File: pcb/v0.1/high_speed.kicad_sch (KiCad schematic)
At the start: 22 parts, among them J4 TYPE_C_Receptacle, J5 TYPE_C_Receptacle, J6 22s_disp_connector, J7 ComputeModule5-CM5_connector, U2 Nexperia PUSB3FR4Z, U3 Nexperia PUSB3FR4Z, U8 AP22653W6-7

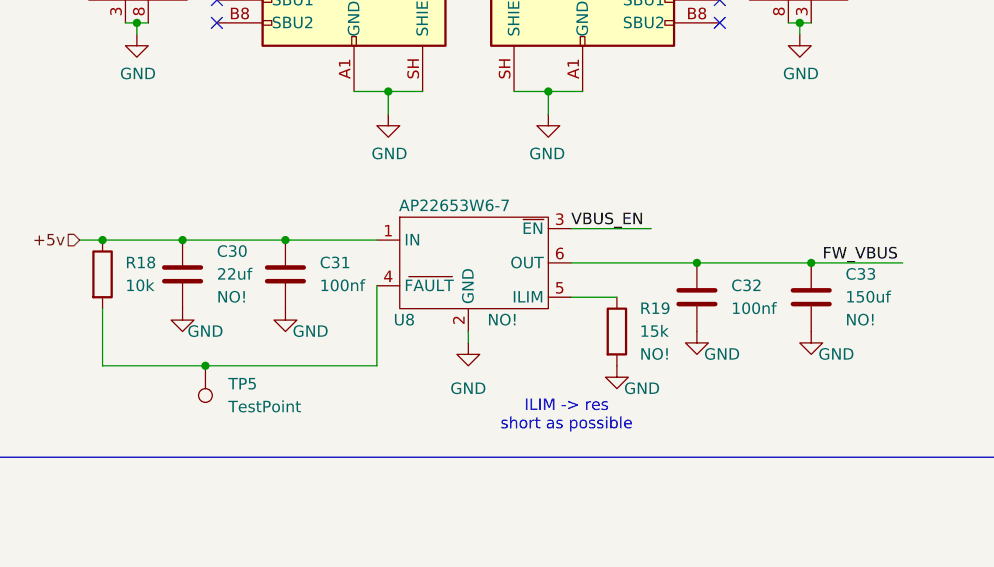
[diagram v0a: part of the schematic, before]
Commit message: Assigned all the footprints
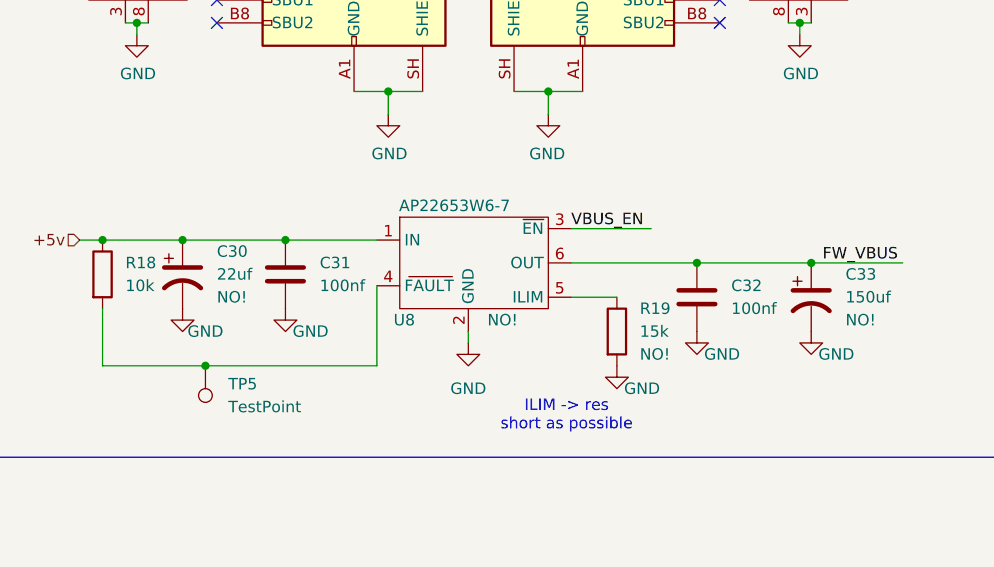
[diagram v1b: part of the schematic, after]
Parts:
- C30: footprint (none) -> Capacitor_SMD:CP_Elec_5x5.3
- C33: footprint (none) -> Capacitor_SMD:CP_Elec_8x10.5
- J4, J5: footprint (none) -> Connector_USB:USB_C_Receptacle_Molex_105450-0101
- J6: footprint (none) -> Connector_PinHeader_2.54mm:PinHeader_1x04_P2.54mm_Vertical
- J7: footprint (none) -> CM5IO:Raspberry-Pi-5-Compute-Module
- TP5: footprint (none) -> TestPoint:TestPoint_Pad_D1.0mm
- U2, U3: footprint (none) -> Package_DFN_QFN:Diodes_UDFN-10_1x2.5mm_P0.5mm
- U8: footprint (none) -> Package_TO_SOT_SMD:SOT-23-6
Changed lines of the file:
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@@
 			)
 		)
-		(property "Footprint" ""
+		(property "Footprint" "Connector_USB:USB_C_Receptacle_Molex_105450-0101"
 			(at 200.66 58.42 0)
 			(hide yes)
@@
 			)
 		)
-		(property "Footprint" ""
+		(property "Footprint" "Capacitor_SMD:CP_Elec_5x5.3"
 			(at 186.3852 123.19 0)
 			(hide yes)
@@
 			)
 		)
-		(property "Footprint" ""
+		(property "Footprint" "Package_DFN_QFN:Diodes_UDFN-10_1x2.5mm_P0.5mm"
 			(at 247.65 71.12 0)
 			(hide yes)
@@
 			)
 		)
-		(property "Footprint" ""
+		(property "Footprint" "Package_TO_SOT_SMD:SOT-23-6"
 			(at 209.55 113.03 0)
 			(hide yes)
@@
 			)
 		)
-		(property "Footprint" ""
+		(property "Footprint" "Capacitor_SMD:CP_Elec_8x10.5"
 			(at 256.2352 125.73 0)
 			(hide yes)
@@
 			)
 		)
-		(property "Footprint" ""
+		(property "Footprint" "CM5IO:Raspberry-Pi-5-Compute-Module"
 			(at 67.31 115.57 0)
 			(hide yes)
@@
 			)
 		)
-		(property "Footprint" ""
+		(property "Footprint" "Connector_USB:USB_C_Receptacle_Molex_105450-0101"
 			(at 233.68 58.42 0)
 			(hide yes)
@@
 			)
 		)
-		(property "Footprint" ""
+		(property "Footprint" "TestPoint:TestPoint_Pad_D1.0mm"
 			(at 182.88 129.54 0)
 			(hide yes)
@@
 			)
 		)
-		(property "Footprint" ""
+		(property "Footprint" "Package_DFN_QFN:Diodes_UDFN-10_1x2.5mm_P0.5mm"
 			(at 186.69 71.12 0)
 			(hide yes)
@@
 			)
 		)
-		(property "Footprint" ""
+		(property "Footprint" "Connector_PinHeader_2.54mm:PinHeader_1x04_P2.54mm_Vertical"
 			(at 140.97 190.5 0)
 			(hide yes)

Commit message: Board setup and basic layout grouping
* Added board setup settings according to JLCpcbs manufacturing minimums
  (and generous extra)
* Grouped related components on the pcb
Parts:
- J6: footprint Connector_PinHeader_2.54mm:PinHeader_1x04_P2.54mm_Vertical -> CM5IO:Hirose_FH12-22S-0.5SH_1x22-1MP_P0.50mm_Horizontal
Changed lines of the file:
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@@
 			)
 		)
-		(property "Footprint" "Connector_PinHeader_2.54mm:PinHeader_1x04_P2.54mm_Vertical"
+		(property "Footprint" "CM5IO:Hirose_FH12-22S-0.5SH_1x22-1MP_P0.50mm_Horizontal"
 			(at 140.97 190.5 0)
 			(hide yes)

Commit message: Remove USB Type-c ports + minor changes + dru file
The current USB type-c ports aren't properly routable without using via
in pad, which at the current stage is prohibitively expensive. I've
removed them for now with the intent of swapping them out for ones from
GTC.

Additionally I noticed that a dru file has not been committed this whole
time. Its existed for a while on my computer.
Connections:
- net USB3-0-RX_N: now also U2.10 (NC)
- net USB3-0-RX_P: now also U2.9 (NC)
- net USB3-0-TX_N: now also U2.7 (NC)
- net USB3-0-TX_P: now also U2.6 (NC)
- net USB3-1-RX_N: now also U3.10 (NC)
- net USB3-1-RX_P: now also U3.9 (NC)
- net USB3-1-TX_N: now also U3.7 (NC)
- net USB3-1-TX_P: now also U3.6 (NC)

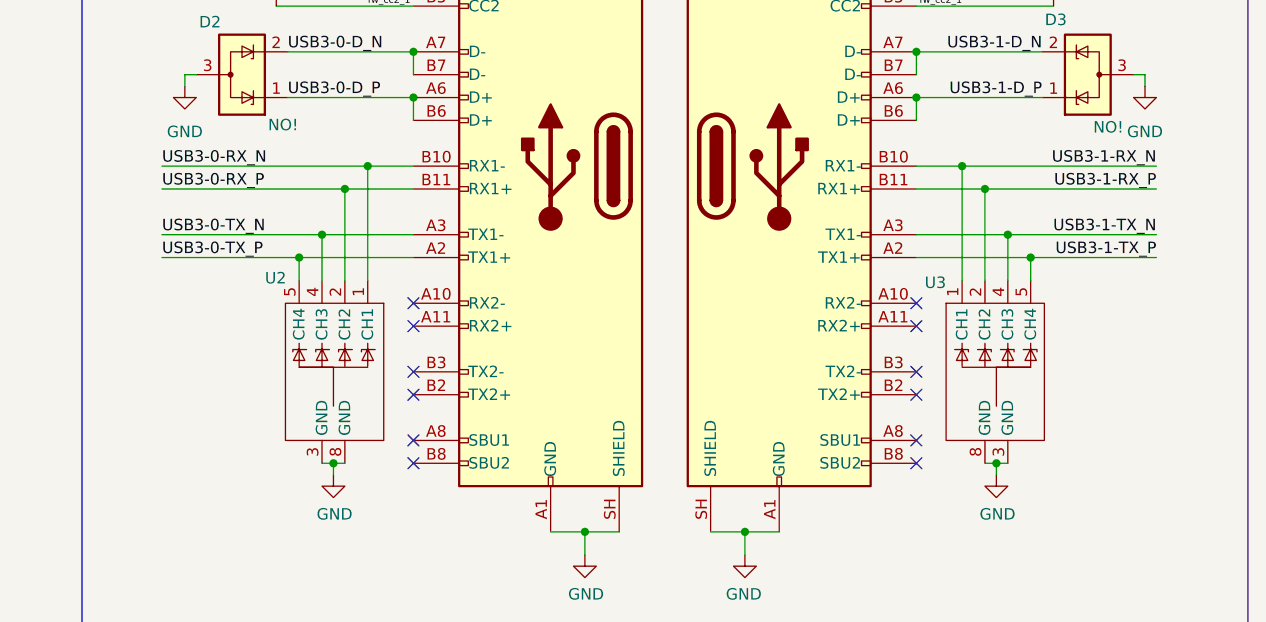
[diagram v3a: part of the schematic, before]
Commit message: USB differential pairs complete.
Had to break these out from the rest of the pcb as they just didn't add
up otherwise. Will continue to do the high speed lines separately before
re assembling the pcb.
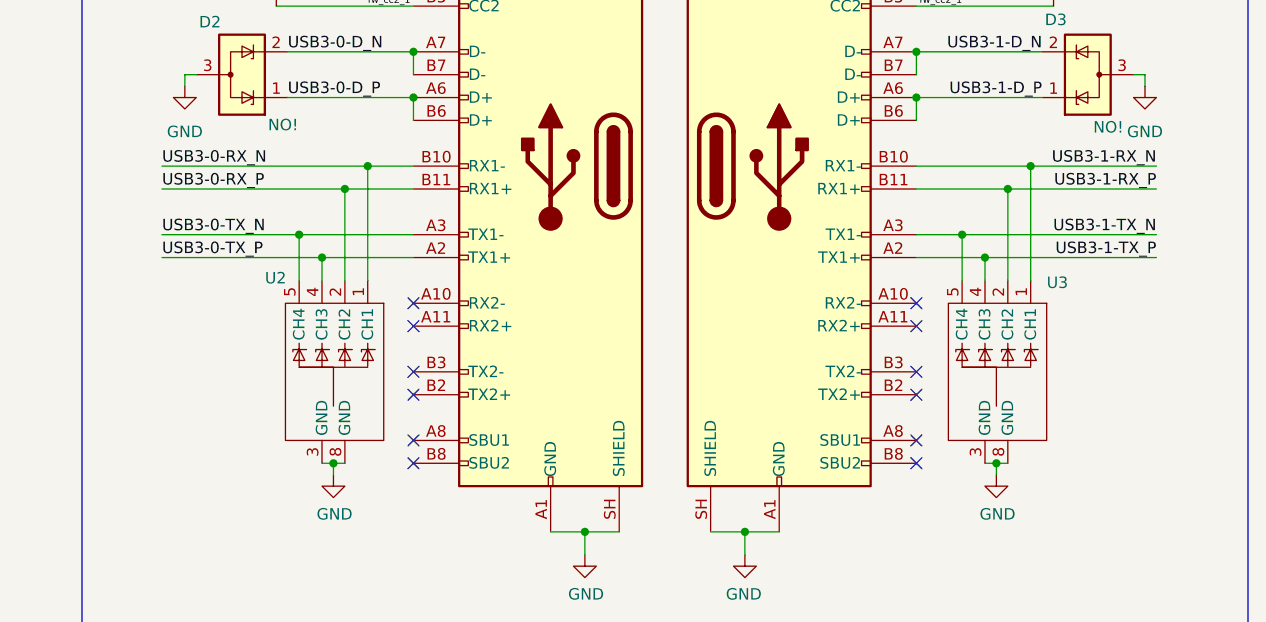
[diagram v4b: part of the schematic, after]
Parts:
- J4, J5: footprint Connector_USB:USB_C_Receptacle_Molex_105450-0101 -> TH-1-CC_footprints:USB4056-03-A; Digikey Part no WM12856TR-ND -> 2073-USB4056-03-ATR-ND; Distributor Digikey https://www.digikey.co.uk/en/products/detail/molex/10545001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 -> https://www.digikey.co.uk/en/products/detail/gct/USB4056-03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; Manufacturer MOLEX -> GCT; Mfr. Part no 1054500101 -> USB4056-03-A
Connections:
- net USB3-0-TX_N: now also U2.5 (CH4), U2.6 (NC); no longer U2.4 (CH3), U2.7 (NC)
- net USB3-0-TX_P: now also U2.4 (CH3), U2.7 (NC); no longer U2.5 (CH4), U2.6 (NC)
- net USB3-1-TX_N: now also U3.5 (CH4), U3.6 (NC); no longer U3.4 (CH3), U3.7 (NC)
- net USB3-1-TX_P: now also U3.4 (CH3), U3.7 (NC); no longer U3.5 (CH4), U3.6 (NC)
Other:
- moved on the sheet: U3

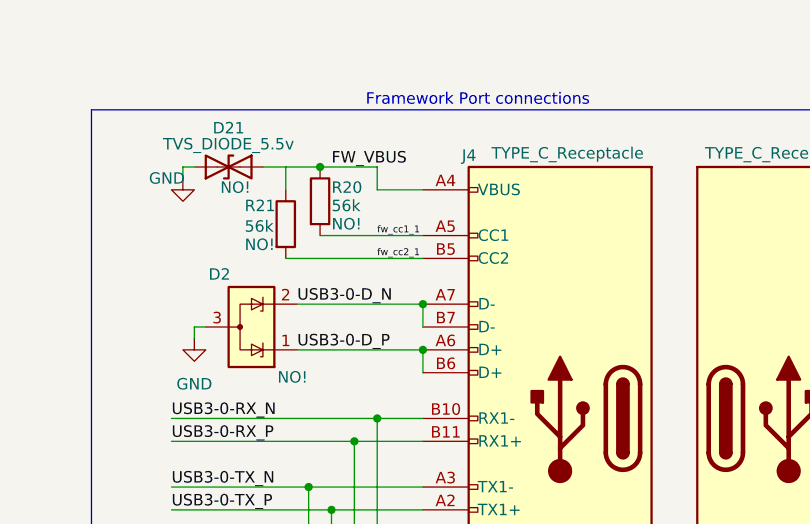
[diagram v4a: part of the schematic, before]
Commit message: New rough layout
Had to change everything up due to the requirements of the high speed
lines. The board is now also a lot smaller
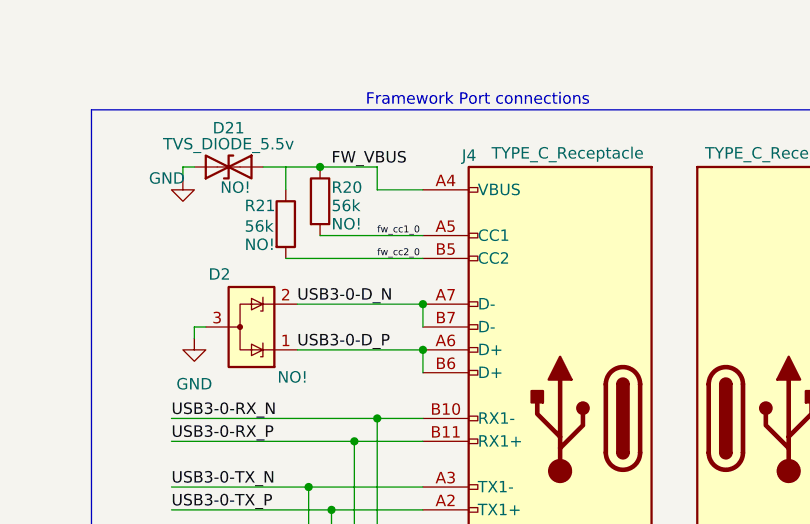
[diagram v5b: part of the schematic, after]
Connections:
- net fw_cc1_1: no longer J4.A5 (CC1), R20.2
- net fw_cc2_1: no longer J4.B5 (CC2), R21.2
- new net fw_cc1_0: J4.A5 (CC1), R20.2
- new net fw_cc2_0: J4.B5 (CC2), R21.2
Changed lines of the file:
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@@
 		)
 	)
-	(label "fw_cc2_1"
+	(label "fw_cc2_0"
 		(at 184.15 40.64 0)
 		(effects
@@
 		)
 	)
-	(label "fw_cc1_1"
+	(label "fw_cc1_0"
 		(at 184.15 38.1 0)
 		(effects

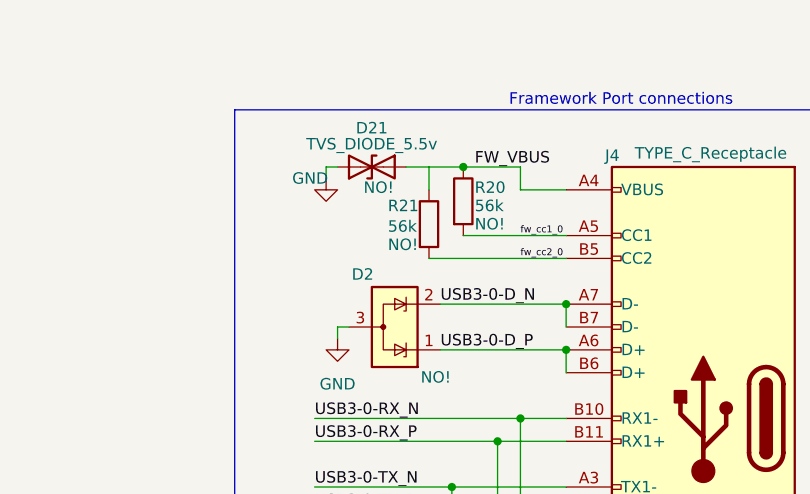
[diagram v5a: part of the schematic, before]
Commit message: A large chunk of the pcb routing + shrinking the board
Did a large chunk of the PCB routing, probably just under half of all
remaining traces. Additionally I shrank the pcb to below 100x100 as it
reduces the price of manufacturing by roughly 4x
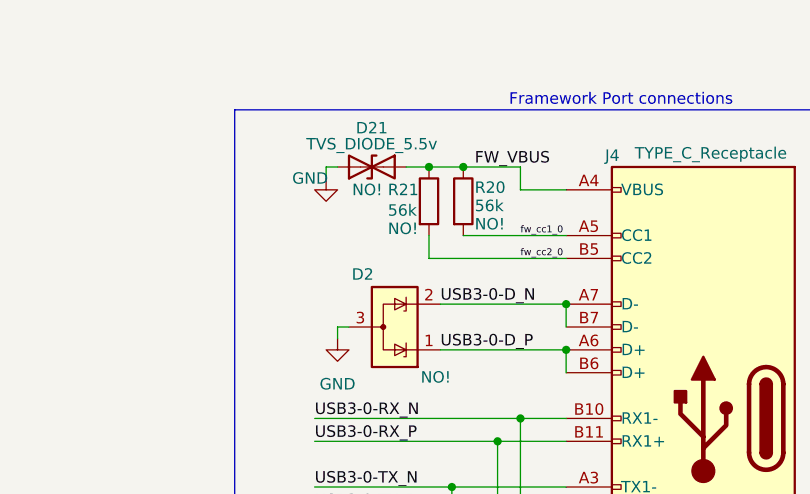
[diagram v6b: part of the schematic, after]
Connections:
- net FW_VBUS: now also R21.1
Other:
- moved on the sheet: R21
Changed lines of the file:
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@@
 	)
 	(junction
+		(at 173.99 30.48)
+		(diameter 0)
+		(color 0 0 0 0)
+	)
+	(junction
 		(at 31.75 66.04)
 		(diameter 1.016)
@@
 	(wire
 		(pts
+			(xy 173.99 30.48) (xy 177.8 30.48)
+		)
+		(stroke
+			(width 0)
+			(type default)
+		)
+	)
+	(wire
+		(pts
 			(xy 31.75 73.66) (xy 34.29 73.66)
 		)
@@
 	(wire
 		(pts
-			(xy 171.45 30.48) (xy 177.8 30.48)
+			(xy 171.45 30.48) (xy 173.99 30.48)
 		)
 		(stroke
@@
 	(wire
 		(pts
-			(xy 173.99 33.02) (xy 173.99 30.48)
+			(xy 173.99 38.1) (xy 173.99 40.64)
 		)
 		(stroke
@@
 	(wire
 		(pts
+			(xy 173.99 40.64) (xy 189.23 40.64)
+		)
+		(stroke
+			(width 0)
+			(type default)
+		)
+	)
+	(wire
+		(pts
 			(xy 242.57 118.11) (xy 255.27 118.11)
 		)
@@
 	(wire
 		(pts
-			(xy 173.99 40.64) (xy 189.23 40.64)
-		)
-		(stroke
-			(width 0)
-			(type default)
-		)
-	)
-	(wire
-		(pts
 			(xy 95.25 127) (xy 97.79 127)
 		)
@@
 	(symbol
 		(lib_id "TH-1-CC:R_56k")
-		(at 173.99 36.83 0)
+		(at 173.99 34.29 0)
 		(unit 1)
 		(body_style 1)
@@
 		(dnp no)
 		(property "Reference" "R21"
-			(at 169.418 34.798 0)
+			(at 169.418 33.02 0)
 			(show_name no)
 			(do_not_autoplace no)
@@
 		)
 		(property "Value" "56k"
-			(at 169.418 37.084 0)
+			(at 169.418 35.306 0)
 			(show_name no)
 			(do_not_autoplace no)
@@
 		)
 		(property "Footprint" "Resistor_SMD:R_0603_1608Metric"
-			(at 172.212 36.83 90)
+			(at 172.212 34.29 90)
 			(hide yes)
 			(show_name no)
@@
 		)
 		(property "Datasheet" "https://www.lcsc.com/datasheet/C114630.pdf?spm=wm.sxq.inf.ggs&lcsc_vid=EwQKAlxRFgdXV1MCRARYXwJRRVZeV1dUEgJXBQFQQgQxVlNeRVFWVVdeT1RaUzsOAxUeFF5JWBYZEEoKFBINSQcJGk4NBhADEA4cHktXRlhXSQwSGg0%3D"
-			(at 173.99 36.83 0)
+			(at 173.99 34.29 0)
 			(hide yes)
 			(show_name no)
@@
 		)
 		(property "Description" "RES 56kΩ ±1% 100mW 0603"
-			(at 173.99 36.83 0)
+			(at 173.99 34.29 0)
 			(hide yes)
 			(show_name no)
@@
 		)
 		(property "Manufacturer" "YAGEO"
-			(at 173.99 36.83 0)
+			(at 173.99 34.29 0)
 			(hide yes)
 			(show_name no)
@@
 		)
 		(property "Mfr. Part No." "RC0603FR-0756KL"
-			(at 173.99 36.83 0)
+			(at 173.99 34.29 0)
 			(hide yes)
 			(show_name no)
@@
 		)
 		(property "Distributor LCSC" "https://www.lcsc.com/product-detail/C114630.html?s_z=n_q_t_56k%25200603"
-			(at 173.99 36.83 0)
+			(at 173.99 34.29 0)
 			(hide yes)
 			(show_name no)
@@
 		)
 		(property "LCSC Part no." "C114630"
-			(at 173.99 36.83 0)
+			(at 173.99 34.29 0)
 			(hide yes)
 			(show_name no)
@@
 		)
 		(property "Stock" "NO!"
-			(at 169.418 39.116 0)
+			(at 169.418 37.338 0)
 			(show_name no)
 			(do_not_autoplace no)
@@
 		)
 		(property "Stock" "NO!"
-			(at 168.402 32.766 0)
+			(at 167.132 33.02 0)
 			(show_name no)
 			(do_not_autoplace no)
